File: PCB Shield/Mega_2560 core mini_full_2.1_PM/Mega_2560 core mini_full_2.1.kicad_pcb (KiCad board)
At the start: 2 copper layers, 89.5 x 59.7 mm, 132 parts, among them P1 2560-core, P10 RX1TX1, P11 Trim, P12 Stick_left, P13 Stick_right, P14 Switch, P15 LCD_I2C, P16 LCD, P17 BATT, P18 Ecolage, P19 Module_TX, P2 Clock, P20 TTL/RS232, P21 Sw_power, P22 JQ6500_28P, P23 Rot_1, P24 Rot_2, P25 Keys, P26 LCD_Alim, P27 HP, P28 5v/3,3v manches, P29 Sw_On, P3 Option, P30 MiniDCDC3A, P31 Pot2, P32 Pot1, P4 Pot3, P5 Vibreur, P6 Micro_sd, P7 SPIX, P8 Audio, P9 SPI, Q1 BSS84, U1 74LVC1G3157GV, U2 TLP290, U3 TLP290, U4 PM5033, U5 LD1117S33TR, U6 MCP604-I/SL, U7 FM24W256, U8 DS3231SN

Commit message: Update pcb files v2.1
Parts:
- added P33: 5V_CODERS, Pin_Headers:Pin_Header_Straight_1x02_Pitch2.54mm, F.Cu at (218.7, 115.2)
- added R10: 100, Resistors_SMD:R_1206, B.Cu at (156.3, 67.3)
- added R18: 200, Resistors_SMD:R_1206, B.Cu at (211.0, 92.1)
- BT1: moved to B.Cu
- RV1: value 220K -> 10K
- RV6: value 22K -> 500
- moved D1 1.05 mm to (208.0, 113.1), turned to 270 degrees
- turned BT1 to 180 degrees
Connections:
- P19 pad 4: Master_PPMout -> Net-(P19-Pad4)
- RV6 pad 2: Net-(P16-Pad18) -> Net-(R10-Pad2)
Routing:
- net Net-(P19-Pad4): track 0.00 -> 13.0 mm
- net PPM16_SIMout: track 32.6 -> 20.2 mm, vias 3 -> 2
- net Master_PPMout: track 29.3 -> 16.9 mm, vias 2 -> 1
- net Net-(P16-Pad18): track 48.1 -> 42.2 mm, vias 4 -> 3
- net Net-(R10-Pad2): track 0.00 -> 5.49 mm
- net Rot_2push: track 28.4 -> 26.8 mm
- net Net-(D1-Pad1): track 13.4 -> 12.1 mm
- net (no net): track 1.25 -> 0.00 mm, vias 1 -> 0
- net VCC: track 421.6 -> 422.8 mm
- net GND: track 142.2 -> 141.6 mm

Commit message: Update pcb files
Remove Master_PPMout in telemetry page
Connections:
- P1 pad B6: Master_PPMout -> (no net)
- R18 pad 2: Master_PPMout -> (no net)
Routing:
- net Master_PPMout: track 16.9 -> 0.00 mm, vias 1 -> 0
- net (no net): track 0.00 -> 16.9 mm, vias 0 -> 1

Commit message: Update pcb files v2.1
Add resistor 220 ohms on signal Tele_RX
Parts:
- added R19: 220, Resistors_SMD:R_1206, F.Cu at (219.0, 94.3)
- moved R18 0.13 mm to (210.9, 92.1)
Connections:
- P1 pad B6: (no net) -> Master_PPMout
- R18 pad 2: (no net) -> Master_PPMout
- U3 pad 3: Tele_RX -> Net-(R19-Pad2)
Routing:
- net (no net): track 16.9 -> 0.00 mm, vias 1 -> 0
- net Master_PPMout: track 0.00 -> 16.8 mm, vias 0 -> 1
- net Net-(R19-Pad2): track 0.00 -> 4.24 mm, vias 0 -> 1
- net Tele_RX: track 39.4 -> 39.7 mm, vias 1 -> 2

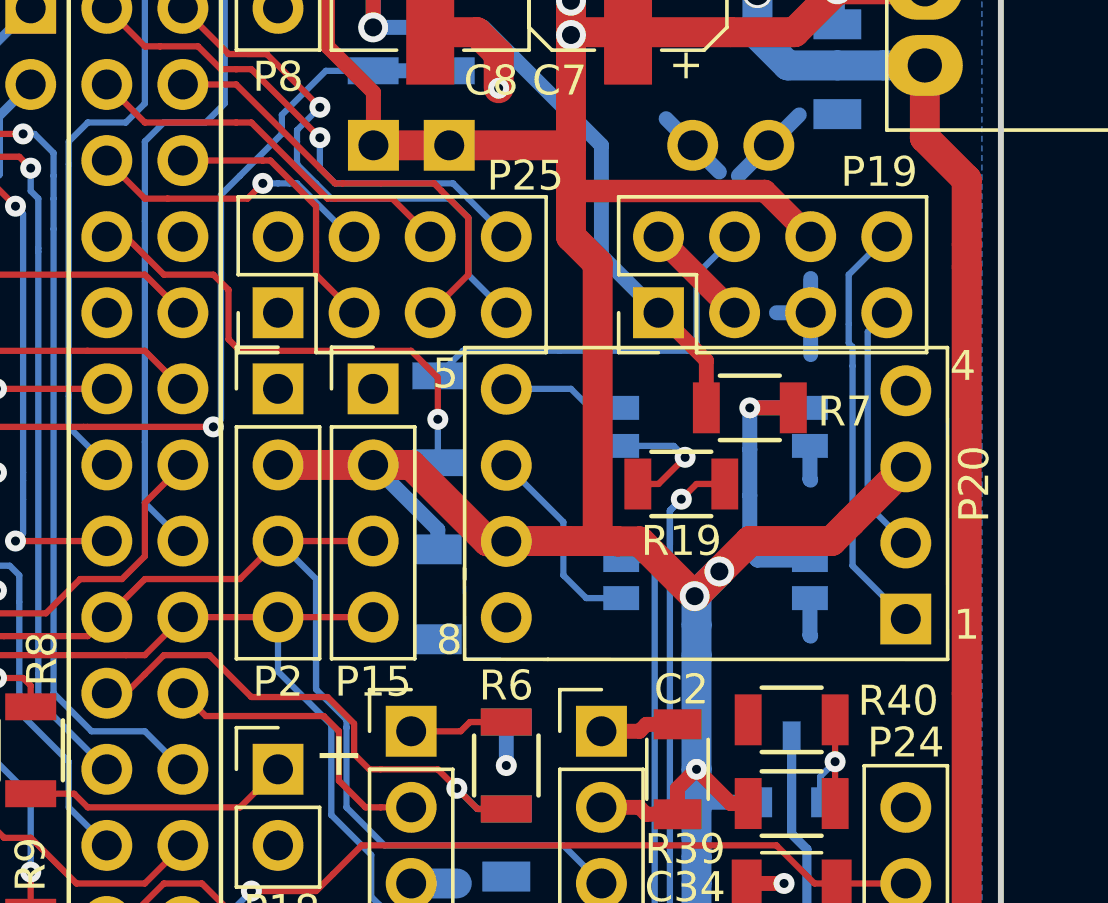
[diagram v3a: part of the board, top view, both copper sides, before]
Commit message: Update schematic & pcb
-modify P19 pinout
-connect Q1 to B7 pin's core
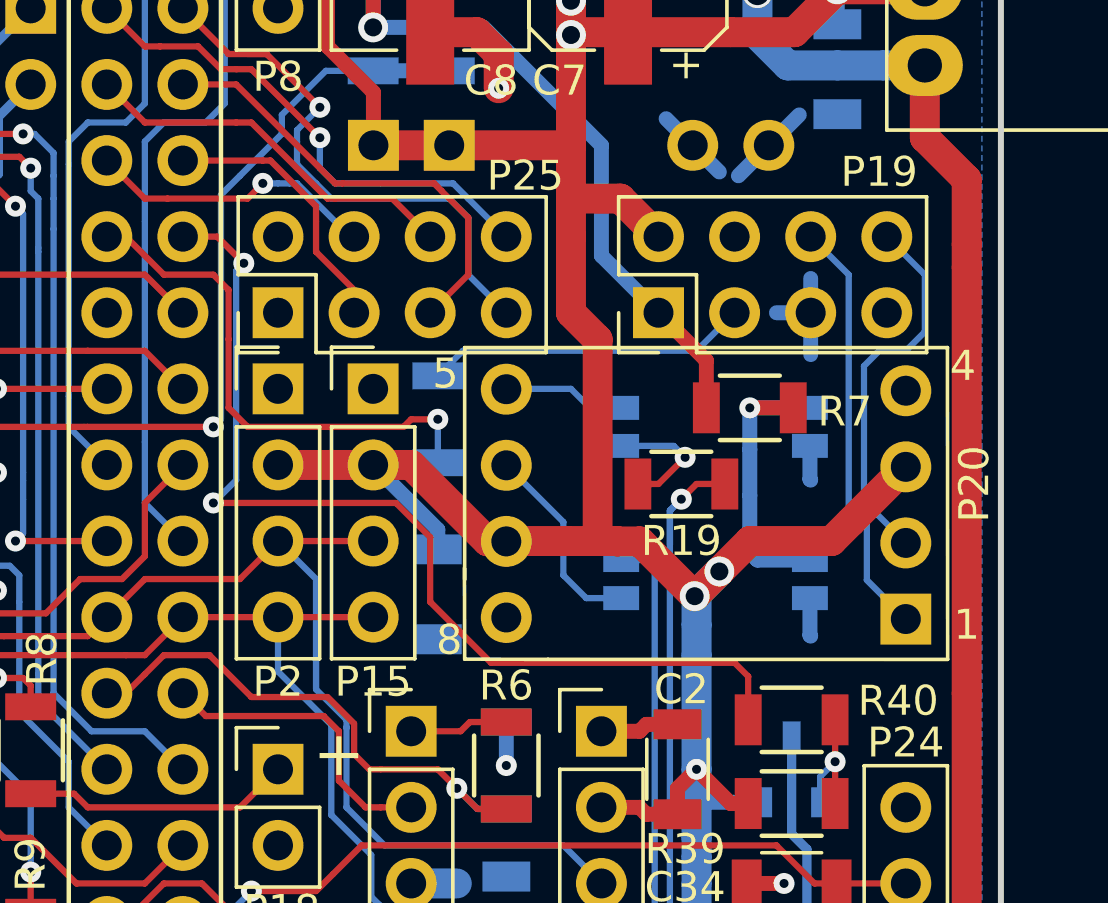
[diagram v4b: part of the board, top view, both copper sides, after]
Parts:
- Q1: value BSS84 -> IRLML5302
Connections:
- P1 pad B7: (no net) -> BT_OnOff
- P19 pad 2: Net-(P19-Pad2) -> VCC
- P19 pad 3: Net-(P19-Pad2) -> Net-(P19-Pad3)
- P19 pad 4: Net-(P19-Pad4) -> GND
- P19 pad 6: VCC -> /OpenAVRc_HF_Telemetry/RX_module
- P19 pad 7: /OpenAVRc_HF_Telemetry/TX_module -> (no net)
- P19 pad 8: /OpenAVRc_HF_Telemetry/RX_module -> /OpenAVRc_HF_Telemetry/TX_module
- R18 pad 1: Net-(P19-Pad4) -> Net-(P19-Pad3)
- R40 pad 1: (no net) -> BT_OnOff
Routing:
- net BT_OnOff: track 0.00 -> 33.8 mm, vias 0 -> 2
- net Net-(P19-Pad4): track 13.2 -> 0.00 mm
- net Net-(P19-Pad3): track 0.00 -> 10.8 mm
- net VCC: track 422.8 -> 417.5 mm
- net /OpenAVRc_HF_Telemetry/TX_module: track 8.47 -> 12.7 mm
- net Net-(P19-Pad2): track 3.59 -> 0.00 mm
- net Master_PPMout: track 16.8 -> 17.5 mm

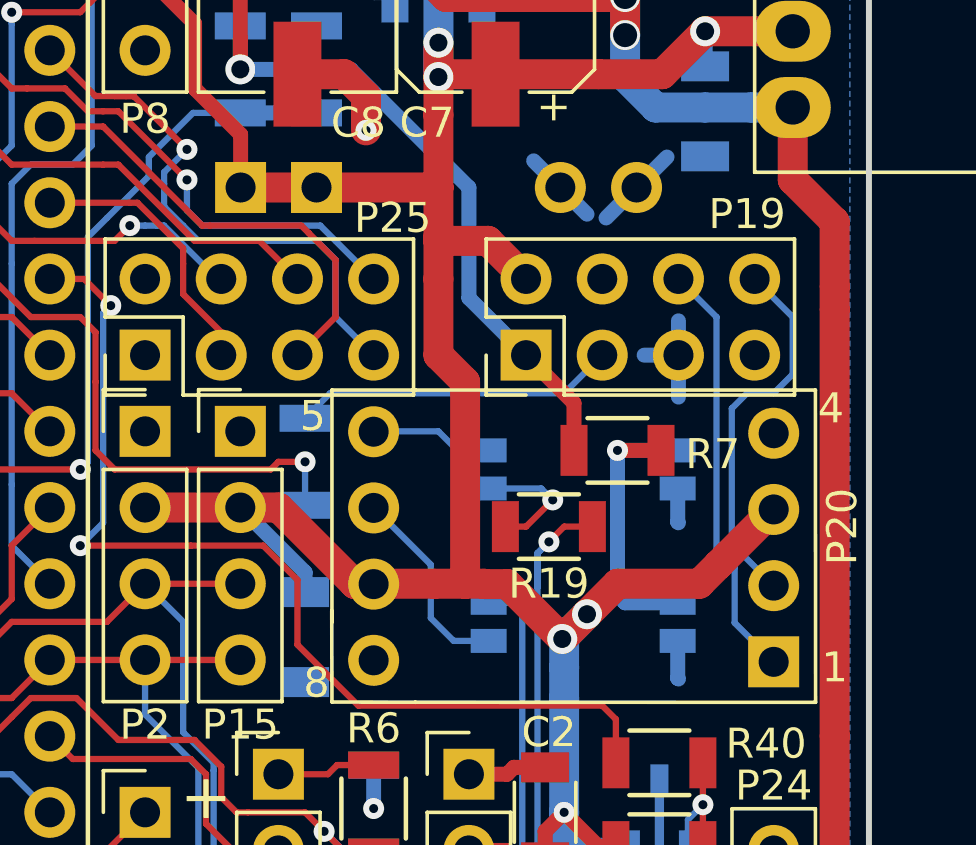
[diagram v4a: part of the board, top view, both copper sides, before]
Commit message: Update schemtaic & PCB files
-update P19 pinout .
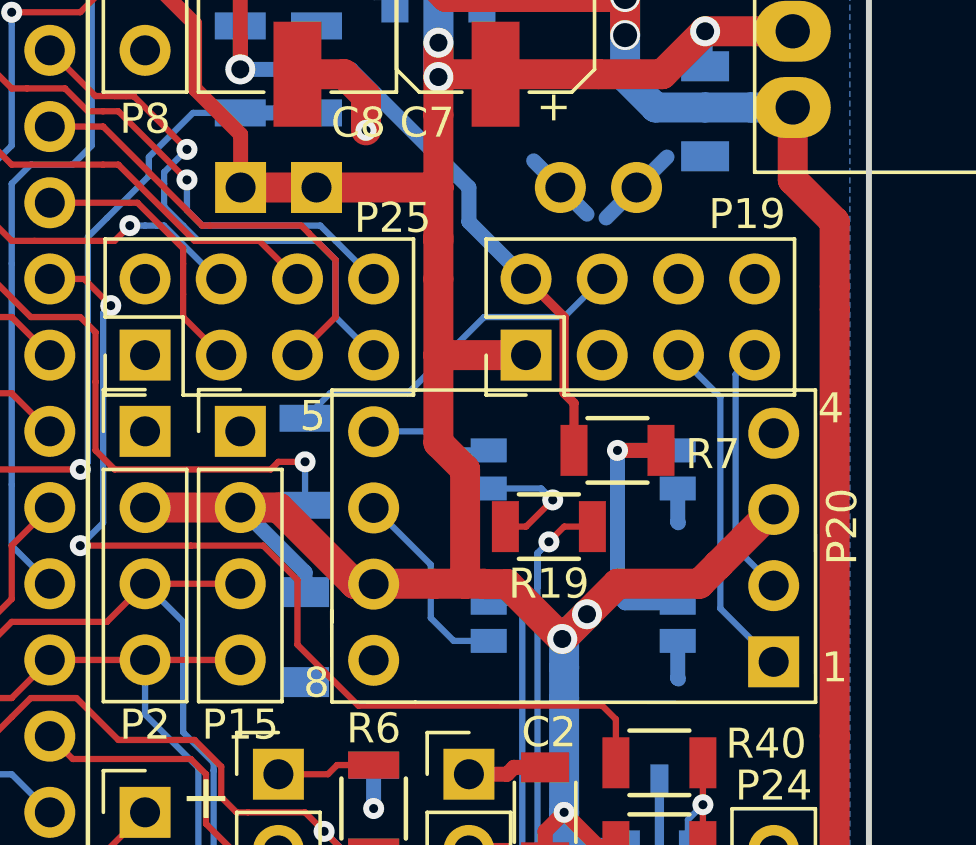
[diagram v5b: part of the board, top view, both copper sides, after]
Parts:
- Q1: value IRLML5302 -> IRLML5203
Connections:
- P19 pad 1: +BATT -> VCC
- P19 pad 2: VCC -> +BATT
- P19 pad 3: Net-(P19-Pad3) -> GND
- P19 pad 4: GND -> Net-(P19-Pad4)
- P19 pad 5: GND -> /OpenAVRc_HF_Telemetry/RX_module
- P19 pad 6: /OpenAVRc_HF_Telemetry/RX_module -> GND
- P19 pad 7: (no net) -> /OpenAVRc_HF_Telemetry/TX_module
- P19 pad 8: /OpenAVRc_HF_Telemetry/TX_module -> (no net)
- R18 pad 1: Net-(P19-Pad3) -> Net-(P19-Pad4)
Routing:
- net Net-(P19-Pad4): track 0.00 -> 11.8 mm
- net Net-(P19-Pad3): track 10.8 -> 0.00 mm
- net /OpenAVRc_HF_Telemetry/TX_module: track 12.7 -> 8.47 mm
- net GND: track 141.6 -> 137.9 mm
- net /OpenAVRc_HF_Telemetry/RX_module: track 14.1 -> 11.5 mm
- net VCC: track 417.5 -> 417.0 mm

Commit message: Update shematic & PCB files
- replace mcp604 by a mcp6004.
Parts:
- U6: value MCP604-I/SL -> MCP6004
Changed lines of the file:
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@@
   )
   (setup
-    (last_trace_width 0.31)
+    (last_trace_width 0.21)
     (user_trace_width 0.31)
     (user_trace_width 0.5)
@@
       (effects (font (size 1 1) (thickness 0.15)))
     )
-    (fp_text value MCP604-I/SL (at -0.381 -2.794 270) (layer F.Fab)
+    (fp_text value MCP6004 (at -0.381 -2.794 270) (layer F.Fab)
       (effects (font (size 1 1) (thickness 0.15)))
     )
@@
   (segment (start 192.47752 81.79448) (end 192.24752 81.56448) (width 1) (layer F.Cu) (net 1) (status 30))
   (segment (start 167.86352 113.94948) (end 169.38752 113.94948) (width 0.5) (layer B.Cu) (net 1))
-  (segment (start 218.28252 88.54948) (end 215.36152 88.54948) (width 1) (layer F.Cu) (net 2) (status 400000))
+  (segment (start 218.28252 88.54948) (end 215.36152 88.54948) (width 1) (layer F.Cu) (net 2))
   (segment (start 215.36152 88.54948) (end 215.36152 91.47048) (width 1) (layer F.Cu) (net 2))
   (segment (start 215.36152 91.47048) (end 216.25052 92.35948) (width 1) (layer F.Cu) (net 2))
@@
   (segment (start 146.52752 98.45548) (end 146.27352 98.70948) (width 0.21) (layer F.Cu) (net 6))
   (segment (start 145.25752 98.70948) (end 146.27352 98.70948) (width 0.21) (layer F.Cu) (net 6) (status 10))
-  (segment (start 219.88052 91.72448) (end 219.88052 90.14748) (width 0.31) (layer F.Cu) (net 7) (status 400000))
-  (segment (start 219.55252 87.27948) (end 218.28252 86.00948) (width 0.31) (layer F.Cu) (net 7) (status 800000))
+  (segment (start 219.88052 91.72448) (end 219.88052 90.14748) (width 0.31) (layer F.Cu) (net 7))
+  (segment (start 219.55252 87.27948) (end 218.28252 86.00948) (width 0.31) (layer F.Cu) (net 7))
   (segment (start 219.55252 89.81948) (end 219.55252 87.27948) (width 0.31) (layer F.Cu) (net 7))
   (segment (start 219.88052 90.14748) (end 219.55252 89.81948) (width 0.31) (layer F.Cu) (net 7))
   (segment (start 216.37752 82.96148) (end 216.37752 84.10448) (width 0.5) (layer B.Cu) (net 7))
-  (segment (start 216.37752 84.10448) (end 218.28252 86.00948) (width 0.5) (layer B.Cu) (net 7) (status 800000))
+  (segment (start 216.37752 84.10448) (end 218.28252 86.00948) (width 0.5) (layer B.Cu) (net 7))
   (segment (start 208.75752 68.22948) (end 208.75752 64.41948) (width 0.5) (layer F.Cu) (net 7))
   (segment (start 212.44052 79.02448) (end 216.37752 82.96148) (width 0.5) (layer B.Cu) (net 7))
@@
   (segment (start 150.97252 116.48948) (end 152.24252 117.75948) (width 0.21) (layer F.Cu) (net 60))
   (segment (start 203.67752 64.41948) (end 200.50252 64.41948) (width 1) (layer F.Cu) (net 61))
-  (segment (start 226.53752 96.23298) (end 225.26752 94.96298) (width 0.21) (layer B.Cu) (net 62) (status 400000))
-  (segment (start 225.26752 89.18448) (end 225.90252 88.54948) (width 0.21) (layer B.Cu) (net 62) (status 800000))
+  (segment (start 226.53752 96.23298) (end 225.26752 94.96298) (width 0.21) (layer B.Cu) (net 62))
+  (segment (start 225.26752 89.18448) (end 225.90252 88.54948) (width 0.21) (layer B.Cu) (net 62))
   (segment (start 225.26752 94.96298) (end 225.26752 89.18448) (width 0.21) (layer B.Cu) (net 62))
-  (segment (start 226.53752 98.77298) (end 224.75952 96.99498) (width 0.21) (layer B.Cu) (net 63) (status 400000))
-  (segment (start 224.75952 89.94648) (end 223.36252 88.54948) (width 0.21) (layer B.Cu) (net 63) (status 800000))
+  (segment (start 226.53752 98.77298) (end 224.75952 96.99498) (width 0.21) (layer B.Cu) (net 63))
+  (segment (start 224.75952 89.94648) (end 223.36252 88.54948) (width 0.21) (layer B.Cu) (net 63))
   (segment (start 224.75952 96.99498) (end 224.75952 89.94648) (width 0.21) (layer B.Cu) (net 63))
   (segment (start 152.64752 111.40948) (end 151.98852 111.40948) (width 0.21) (layer B.Cu) (net 64))
@@
   (segment (start 219.55252 87.27948) (end 216.88552 87.27948) (width 0.21) (layer B.Cu) (net 133))
   (segment (start 216.88552 87.27948) (end 214.34552 89.81948) (width 0.21) (layer B.Cu) (net 133))
-  (segment (start 210.91652 90.65548) (end 211.75252 89.81948) (width 0.21) (layer B.Cu) (net 133) (status 400000))
+  (segment (start 210.91652 90.65548) (end 211.75252 89.81948) (width 0.21) (layer B.Cu) (net 133))
   (segment (start 211.75252 89.81948) (end 214.34552 89.81948) (width 0.21) (layer B.Cu) (net 133))
-  (segment (start 219.55252 87.27948) (end 220.82252 86.00948) (width 0.21) (layer B.Cu) (net 133) (status 800000))
+  (segment (start 219.55252 87.27948) (end 220.82252 86.00948) (width 0.21) (layer B.Cu) (net 133))
   (zone (net 1) (net_name GND) (layer B.Cu) (hatch edge 0.508)
     (connect_pads (clearance 0.21))

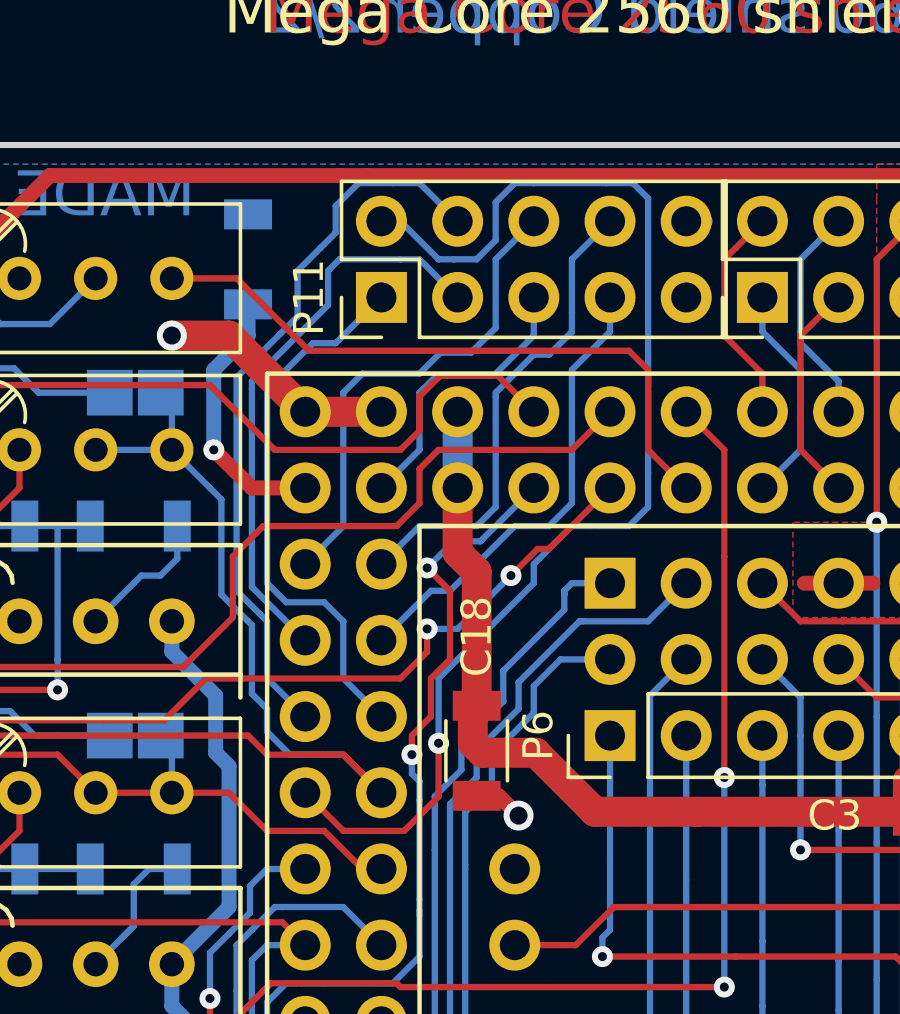
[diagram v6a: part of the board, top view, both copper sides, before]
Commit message: Update schematic & pcb files
- change P11 pin out.
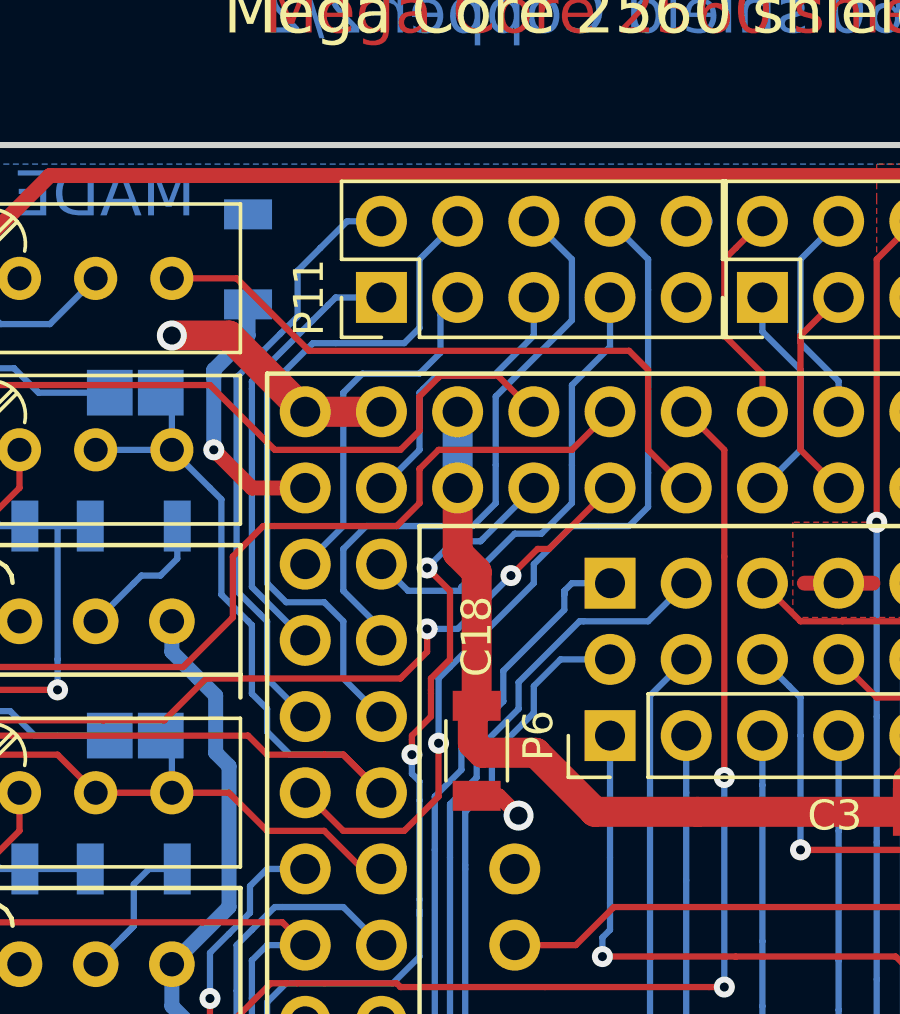
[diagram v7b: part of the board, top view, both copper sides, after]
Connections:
- P11 pad 1: Trim_LH-> -> Trim_RV<-
- P11 pad 2: Trim_LH<- -> Trim_LV<-
- P11 pad 3: Trim_RV<- -> Trim_RH<-
- P11 pad 4: Trim_LV<- -> Trim_LH->
- P11 pad 6: Trim_RH<- -> Trim_LV->
- P11 pad 7: Trim_LV-> -> Trim_RV->
- P11 pad 8: Trim_RV-> -> Trim_LH<-
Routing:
- net Trim_LH<-: track 41.5 -> 29.3 mm
- net Trim_LH->: track 18.3 -> 23.2 mm
- net Trim_LV->: track 15.6 -> 20.3 mm
- net Trim_RV<-: track 19.1 -> 14.8 mm
- net Trim_RH<-: track 16.3 -> 12.1 mm
- net Trim_LV<-: track 24.2 -> 20.1 mm
- net Trim_RV->: track 16.0 -> 15.4 mm
